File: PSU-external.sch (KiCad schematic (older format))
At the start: 32 parts

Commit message: Added component numbers.
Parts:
- gave numbers to parts that had none: 32
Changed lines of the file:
@@
 $EndDescr
 $Comp
-L CP1 C?
+L CP1 C24
 U 1 1 53688F81
 P 7200 4300
-F 0 "C?" H 7250 4400 50  0000 L CNN
+F 0 "C24" H 7250 4400 50  0000 L CNN
 F 1 "5600u" H 7250 4200 50  0000 L CNN
 F 2 "" H 7200 4300 60  0000 C CNN
@@
 $EndComp
 $Comp
-L C C?
+L C C27
 U 1 1 53688F85
 P 7550 4300
-F 0 "C?" H 7550 4400 40  0000 L CNN
+F 0 "C27" H 7550 4400 40  0000 L CNN
 F 1 "100n" H 7556 4215 40  0000 L CNN
 F 2 "~" H 7588 4150 30  0000 C CNN
@@
 -18V_EXT
 $Comp
-L MC7805C U?
+L MC7805C U12
 U 1 1 53688F96
 P 8000 1050
-F 0 "U?" H 7800 1250 40  0000 C CNN
+F 0 "U12" H 7800 1250 40  0000 C CNN
 F 1 "MC7805C" H 8000 1250 40  0000 L CNN
 F 2 "TO-220" H 8000 1150 30  0000 C CIN
@@
 $EndComp
 $Comp
-L CP1 C?
+L CP1 C23
 U 1 1 53688F97
 P 7150 1500
-F 0 "C?" H 7200 1600 50  0000 L CNN
+F 0 "C23" H 7200 1600 50  0000 L CNN
 F 1 "2700u" H 7200 1400 50  0000 L CNN
 F 2 "" H 7150 1500 60  0000 C CNN
@@
 $EndComp
 $Comp
-L C C?
+L C C26
 U 1 1 53688F98
 P 7550 1500
-F 0 "C?" H 7550 1600 40  0000 L CNN
+F 0 "C26" H 7550 1600 40  0000 L CNN
 F 1 "100n" H 7556 1415 40  0000 L CNN
 F 2 "~" H 7588 1350 30  0000 C CNN
@@
 +20.5V min
 $Comp
-L CP1 C?
+L CP1 C25
 U 1 1 53688FA0
 P 7200 5250
-F 0 "C?" H 7250 5350 50  0000 L CNN
+F 0 "C25" H 7250 5350 50  0000 L CNN
 F 1 "5600u" H 7250 5150 50  0000 L CNN
 F 2 "" H 7200 5250 60  0000 C CNN
@@
 $EndComp
 $Comp
-L C C?
+L C C28
 U 1 1 53688FA4
 P 7550 5250
-F 0 "C?" H 7550 5350 40  0000 L CNN
+F 0 "C28" H 7550 5350 40  0000 L CNN
 F 1 "100n" H 7556 5165 40  0000 L CNN
 F 2 "~" H 7588 5100 30  0000 C CNN
@@
 SAF_GND
 $Comp
-L DIODE D?
+L DIODE D9
 U 1 1 5368E09A
 P 6750 1200
-F 0 "D?" H 6750 1300 40  0000 C CNN
+F 0 "D9" H 6750 1300 40  0000 C CNN
 F 1 "1N4001" H 6750 1100 40  0000 C CNN
 F 2 "~" H 6750 1200 60  0000 C CNN
@@
 $EndComp
 $Comp
-L DIODE D?
+L DIODE D5
 U 1 1 5368E121
 P 6400 1200
-F 0 "D?" H 6400 1300 40  0000 C CNN
+F 0 "D5" H 6400 1300 40  0000 C CNN
 F 1 "1N4001" H 6400 1100 40  0000 C CNN
 F 2 "~" H 6400 1200 60  0000 C CNN
@@
 $EndComp
 $Comp
-L DIODE D?
+L DIODE D6
 U 1 1 5368E163
 P 6400 1800
-F 0 "D?" H 6400 1900 40  0000 C CNN
+F 0 "D6" H 6400 1900 40  0000 C CNN
 F 1 "1N4001" H 6400 1700 40  0000 C CNN
 F 2 "~" H 6400 1800 60  0000 C CNN
@@
 $EndComp
 $Comp
-L DIODE D?
+L DIODE D10
 U 1 1 5368E169
 P 6750 1800
-F 0 "D?" H 6750 1900 40  0000 C CNN
+F 0 "D10" H 6750 1900 40  0000 C CNN
 F 1 "1N4001" H 6750 1700 40  0000 C CNN
 F 2 "~" H 6750 1800 60  0000 C CNN
@@
 $EndComp
 $Comp
-L DIODE D?
+L DIODE D7
 U 1 1 5368E721
 P 6450 3950
-F 0 "D?" H 6450 4050 40  0000 C CNN
+F 0 "D7" H 6450 4050 40  0000 C CNN
 F 1 "RL205" H 6450 3850 40  0000 C CNN
 F 2 "~" H 6450 3950 60  0000 C CNN
@@
 $EndComp
 $Comp
-L DIODE D?
+L DIODE D11
 U 1 1 5368E7AB
 P 6800 3950
-F 0 "D?" H 6800 4050 40  0000 C CNN
+F 0 "D11" H 6800 4050 40  0000 C CNN
 F 1 "RL205" H 6800 3850 40  0000 C CNN
 F 2 "~" H 6800 3950 60  0000 C CNN
@@
 $EndComp
 $Comp
-L DIODE D?
+L DIODE D8
 U 1 1 5368E7B1
 P 6450 5650
-F 0 "D?" H 6450 5750 40  0000 C CNN
+F 0 "D8" H 6450 5750 40  0000 C CNN
 F 1 "RL205" H 6450 5550 40  0000 C CNN
 F 2 "~" H 6450 5650 60  0000 C CNN
@@
 $EndComp
 $Comp
-L DIODE D?
+L DIODE D12
 U 1 1 5368E7B7
 P 6800 5650
-F 0 "D?" H 6800 5750 40  0000 C CNN
+F 0 "D12" H 6800 5750 40  0000 C CNN
 F 1 "RL205" H 6800 5550 40  0000 C CNN
 F 2 "~" H 6800 5650 60  0000 C CNN
@@
 $EndComp
 $Comp
-L C C?
+L C C22
 U 1 1 536984D3
 P 6200 4500
-F 0 "C?" H 6200 4600 40  0000 L CNN
+F 0 "C22" H 6200 4600 40  0000 L CNN
 F 1 "C" H 6206 4415 40  0000 L CNN
 F 2 "~" H 6238 4350 30  0000 C CNN
@@
 $EndComp
 $Comp
-L R R?
+L R R22
 U 1 1 536984E2
 P 6200 5100
-F 0 "R?" V 6280 5100 40  0000 C CNN
+F 0 "R22" V 6280 5100 40  0000 C CNN
 F 1 "R" V 6207 5101 40  0000 C CNN
 F 2 "~" V 6130 5100 30  0000 C CNN
@@
 $EndComp
 $Comp
-L C C?
+L C C21
 U 1 1 5369950E
 P 5800 1200
-F 0 "C?" H 5800 1300 40  0000 L CNN
+F 0 "C21" H 5800 1300 40  0000 L CNN
 F 1 "C" H 5806 1115 40  0000 L CNN
 F 2 "~" H 5838 1050 30  0000 C CNN
@@
 $EndComp
 $Comp
-L R R?
+L R R21
 U 1 1 53699514
 P 5800 1750
-F 0 "R?" V 5880 1750 40  0000 C CNN
+F 0 "R21" V 5880 1750 40  0000 C CNN
 F 1 "R" V 5807 1751 40  0000 C CNN
 F 2 "~" V 5730 1750 30  0000 C CNN
@@
 	6400 2000 8850 2000
 $Comp
-L TRIAD-FS48-750-C2 T?
+L TRIAD-FS48-750-C2 T2
 U 1 1 5369B344
 P 4600 4800
-F 0 "T?" H 4600 5300 70  0000 C CNN
+F 0 "T2" H 4600 5300 70  0000 C CNN
 F 1 "TRIAD-FS48-750-C2" H 4600 4300 70  0000 C CNN
 F 2 "" H 4600 4800 60  0000 C CNN
@@
 $EndComp
 $Comp
-L TRIAD-FS16-400-C2 T?
+L TRIAD-FS16-400-C2 T1
 U 1 1 5369B6AF
 P 4600 1500
-F 0 "T?" H 4600 2000 70  0000 C CNN
+F 0 "T1" H 4600 2000 70  0000 C CNN
 F 1 "TRIAD-FS16-400-C2" H 4600 1000 70  0000 C CNN
 F 2 "" H 4600 1500 60  0000 C CNN
@@
 	5000 1400 5000 1600
 $Comp
-L IEC-C13-SOCKET J?
+L IEC-C13-SOCKET J3
 U 1 1 5369A60D
 P 2600 3700
-F 0 "J?" H 2350 3000 60  0000 L CNN
+F 0 "J3" H 2350 3000 60  0000 L CNN
 F 1 "IEC-C13-SOCKET" H 2350 2900 60  0000 L CNN
 F 2 "~" H 2550 4100 60  0000 C CNN
@@
 Connection ~ 3700 4250
 $Comp
-L LM7918CT U?
+L LM7918CT U14
 U 1 1 5369BF38
 P 8000 5800
-F 0 "U?" H 7800 5600 40  0000 C CNN
+F 0 "U14" H 7800 5600 40  0000 C CNN
 F 1 "LM7918CT" H 8000 5600 40  0000 L CNN
 F 2 "TO-220" H 8000 5700 30  0000 C CIN
@@
 $EndComp
 $Comp
-L LM7818CT U?
+L LM7818CT U13
 U 1 1 5369BF47
 P 8000 3800
-F 0 "U?" H 7800 4000 40  0000 C CNN
+F 0 "U13" H 7800 4000 40  0000 C CNN
 F 1 "LM7818CT" H 8000 4000 40  0000 L CNN
 F 2 "TO-220" H 8000 3900 30  0000 C CIN
@@
 $EndComp
 $Comp
-L DIODE D?
+L DIODE D13
 U 1 1 5369C01A
 P 8000 650
-F 0 "D?" H 8000 750 40  0000 C CNN
+F 0 "D13" H 8000 750 40  0000 C CNN
 F 1 "1N4001" H 8000 550 40  0000 C CNN
 F 2 "~" H 8000 650 60  0000 C CNN
@@
 Connection ~ 7450 1000
 $Comp
-L DIODE D?
+L DIODE D14
 U 1 1 5369C0E9
 P 8000 3400
-F 0 "D?" H 8000 3500 40  0000 C CNN
+F 0 "D14" H 8000 3500 40  0000 C CNN
 F 1 "1N4001" H 8000 3300 40  0000 C CNN
 F 2 "~" H 8000 3400 60  0000 C CNN
@@
 Connection ~ 8500 3750
 $Comp
-L DIODE D?
+L DIODE D15
 U 1 1 5369C1C4
 P 8000 6200
-F 0 "D?" H 8000 6300 40  0000 C CNN
+F 0 "D15" H 8000 6300 40  0000 C CNN
 F 1 "1N4001" H 8000 6100 40  0000 C CNN
 F 2 "~" H 8000 6200 60  0000 C CNN
@@
 Connection ~ 8500 5850
 $Comp
-L CP1 C?
+L CP1 C30
 U 1 1 5369C418
 P 8450 4300
-F 0 "C?" H 8500 4400 50  0000 L CNN
+F 0 "C30" H 8500 4400 50  0000 L CNN
 F 1 "1u" H 8500 4200 50  0000 L CNN
 F 2 "" H 8450 4300 60  0000 C CNN
@@
 Connection ~ 8450 4800
 $Comp
-L CP1 C?
+L CP1 C31
 U 1 1 5369C517
 P 8450 5250
-F 0 "C?" H 8500 5350 50  0000 L CNN
+F 0 "C31" H 8500 5350 50  0000 L CNN
 F 1 "1u" H 8500 5150 50  0000 L CNN
 F 2 "" H 8450 5250 60  0000 C CNN
@@
 Connection ~ 8450 5850
 $Comp
-L CP1 C?
+L CP1 C29
 U 1 1 5369C772
 P 8450 1500
-F 0 "C?" H 8500 1600 50  0000 L CNN
+F 0 "C29" H 8500 1600 50  0000 L CNN
 F 1 "1u" H 8500 1400 50  0000 L CNN
 F 2 "" H 8450 1500 60  0000 C CNN
@@
 	5000 5200 5000 5350
 $Comp
-L SMP50 U?
+L SMP50 U10
 U 1 1 536F40A7
 P 5350 2450
-F 0 "U?" H 5500 2350 60  0000 L CNN
+F 0 "U10" H 5500 2350 60  0000 L CNN
 F 1 "SMP50" H 5500 2250 60  0000 L CNN
 F 2 "" H 5350 2500 60  0000 C CNN
@@
 $EndComp
 $Comp
-L SMP50 U?
+L SMP50 U11
 U 1 1 536F40F8
 P 5400 3650
-F 0 "U?" H 5550 3550 60  0000 L CNN
+F 0 "U11" H 5550 3550 60  0000 L CNN
 F 1 "SMP50" H 5550 3450 60  0000 L CNN
 F 2 "" H 5400 3700 60  0000 C CNN

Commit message: More packages specified; changed the external PSU overvoltage protection devices.
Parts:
- removed U10, U11: SMP50, symbol SMP50
- added U? (x2): P0720ECL, ~, symbol P0720ECL
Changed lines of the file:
@@
 Wire Wire Line
 	5000 5200 5000 5350
-$Comp
-L SMP50 U10
-U 1 1 536F40A7
-P 5350 2450
-F 0 "U10" H 5500 2350 60  0000 L CNN
-F 1 "SMP50" H 5500 2250 60  0000 L CNN
-F 2 "" H 5350 2500 60  0000 C CNN
-F 3 "" H 5350 2500 60  0000 C CNN
-F 4 "497-6526-1-ND" H 5350 2450 60  0001 C CNN "DigiKey"
-	1    5350 2450
-	1    0    0    -1
-$EndComp
-$Comp
-L SMP50 U11
-U 1 1 536F40F8
-P 5400 3650
-F 0 "U11" H 5550 3550 60  0000 L CNN
-F 1 "SMP50" H 5550 3450 60  0000 L CNN
-F 2 "" H 5400 3700 60  0000 C CNN
-F 3 "" H 5400 3700 60  0000 C CNN
-F 4 "497-6526-1-ND" H 5400 3650 60  0001 C CNN "DigiKey"
-	1    5400 3650
-	1    0    0    -1
-$EndComp
 Wire Wire Line
 	2150 3000 8850 3000
@@
 Wire Wire Line
 	5400 3850 5400 4800
+$Comp
+L P0720ECL U?
+U 1 1 537CB1E3
+P 5350 2450
+F 0 "U?" H 5500 2350 60  0000 L CNN
+F 1 "P0720ECL" H 5500 2250 60  0000 L CNN
+F 2 "~" H 5350 2500 60  0000 C CNN
+F 3 "~" H 5350 2500 60  0000 C CNN
+	1    5350 2450
+	1    0    0    -1
+$EndComp
+$Comp
+L P0720ECL U?
+U 1 1 537CB1F0
+P 5400 3650
+F 0 "U?" H 5550 3550 60  0000 L CNN
+F 1 "P0720ECL" H 5550 3450 60  0000 L CNN
+F 2 "~" H 5400 3700 60  0000 C CNN
+F 3 "~" H 5400 3700 60  0000 C CNN
+	1    5400 3650
+	1    0    0    -1
+$EndComp
 $EndSCHEMATC

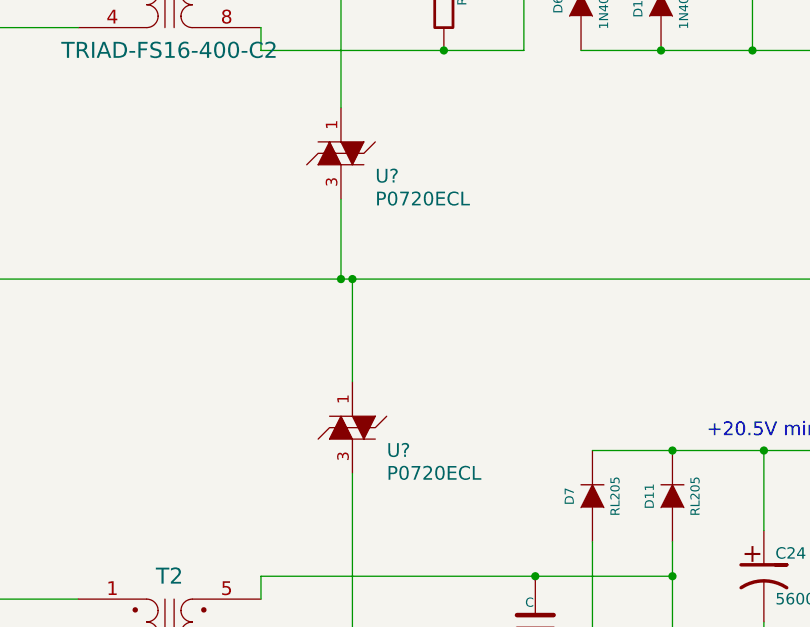
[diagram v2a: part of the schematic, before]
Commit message: More packages specified.
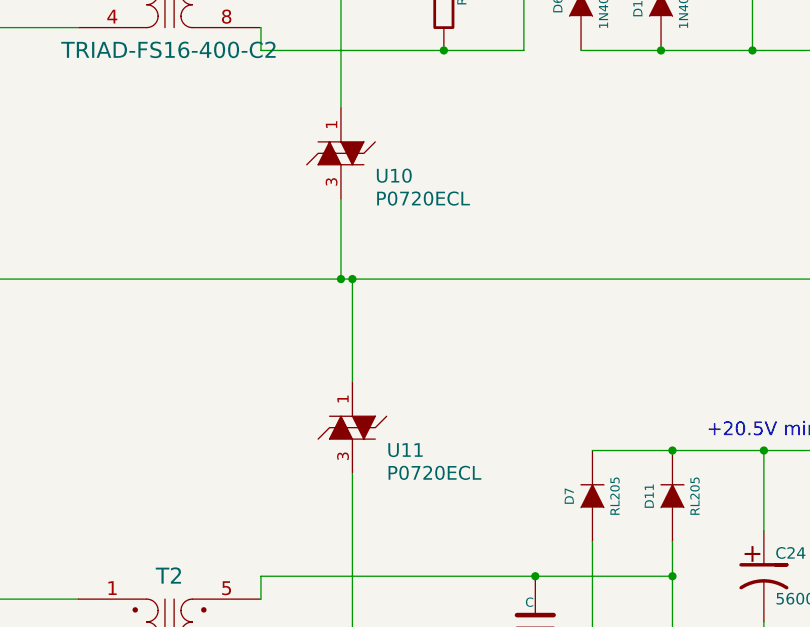
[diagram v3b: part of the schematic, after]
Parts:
- gave numbers to parts that had none: 2
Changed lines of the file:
@@
 	5400 3850 5400 4800
 $Comp
-L P0720ECL U?
+L P0720ECL U10
 U 1 1 537CB1E3
 P 5350 2450
-F 0 "U?" H 5500 2350 60  0000 L CNN
+F 0 "U10" H 5500 2350 60  0000 L CNN
 F 1 "P0720ECL" H 5500 2250 60  0000 L CNN
 F 2 "~" H 5350 2500 60  0000 C CNN
@@
 $EndComp
 $Comp
-L P0720ECL U?
+L P0720ECL U11
 U 1 1 537CB1F0
 P 5400 3650
-F 0 "U?" H 5550 3550 60  0000 L CNN
+F 0 "U11" H 5550 3550 60  0000 L CNN
 F 1 "P0720ECL" H 5550 3450 60  0000 L CNN
 F 2 "~" H 5400 3700 60  0000 C CNN

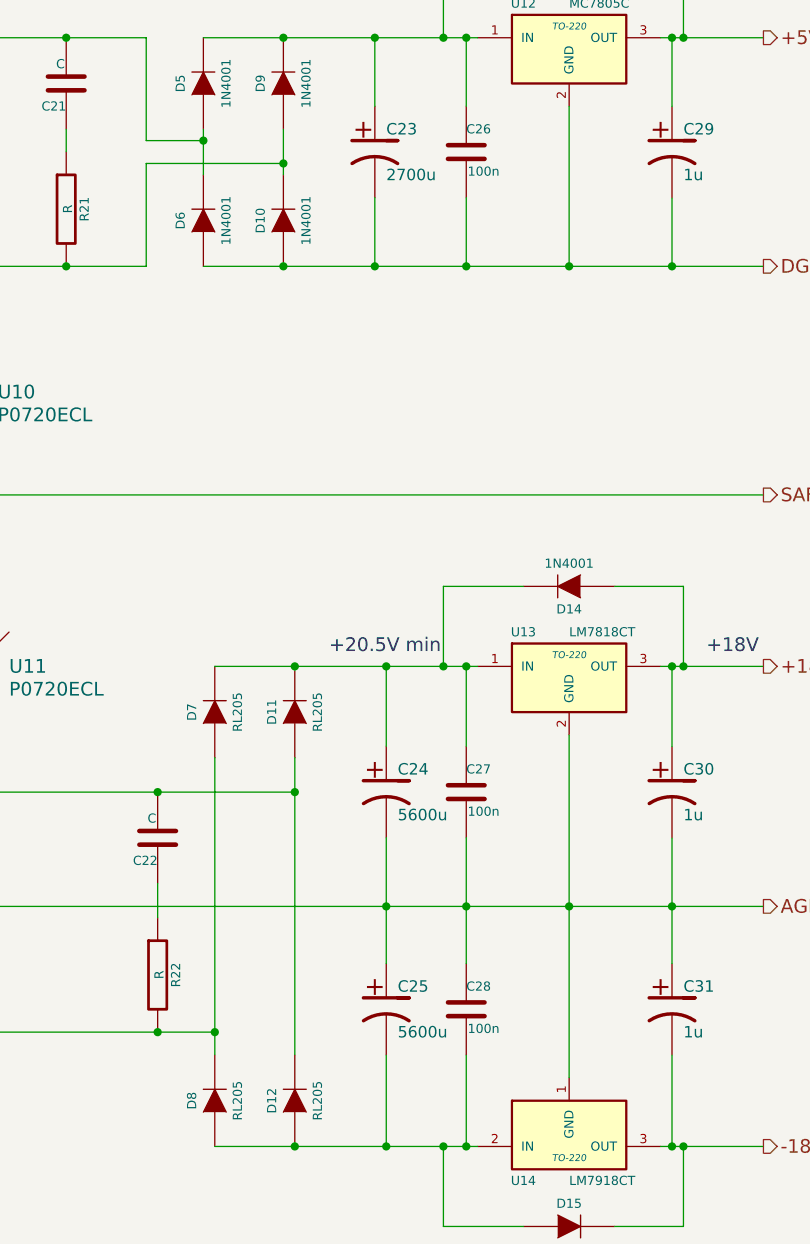
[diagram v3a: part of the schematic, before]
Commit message: Minor schematic mods, started assigning DigiKey part numbers to components.
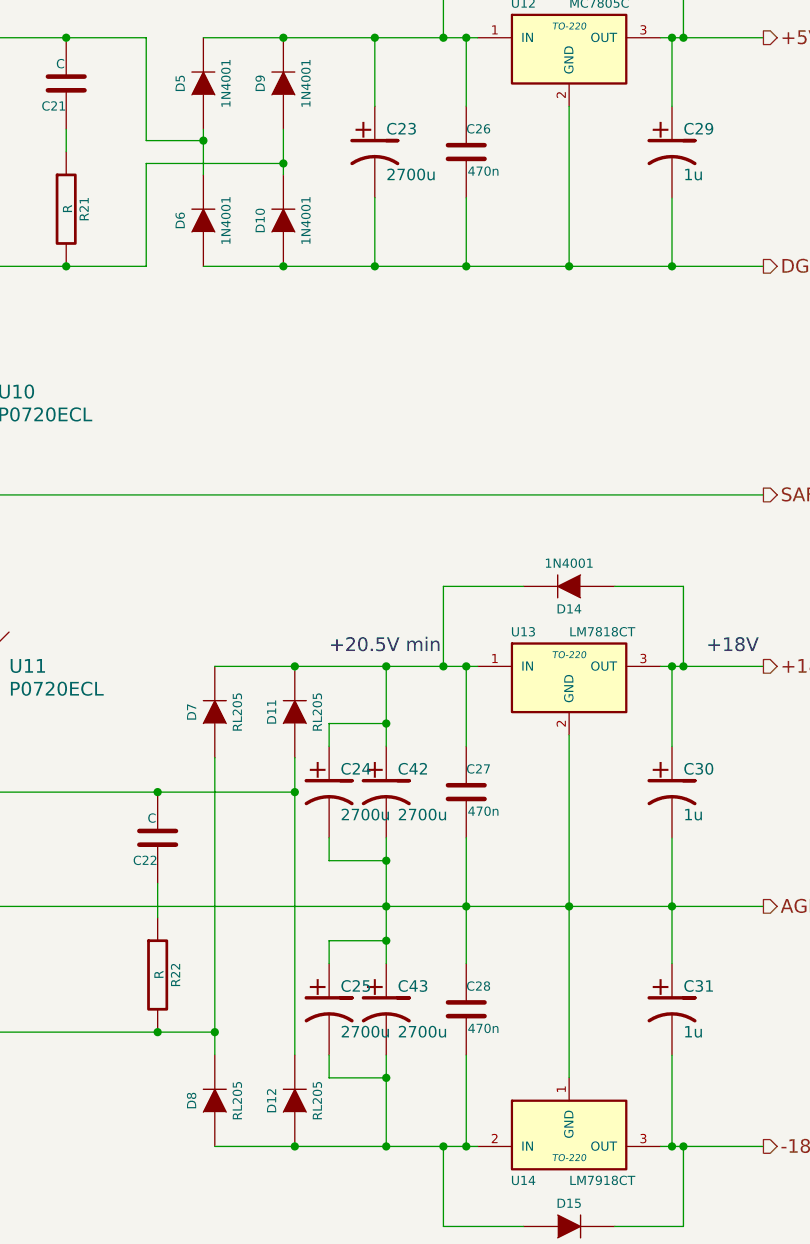
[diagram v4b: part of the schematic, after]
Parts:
- added C42, C43: 2700u, symbol CP1
- C23: DigiKey (none) -> 565-1830-ND
- C24, C25: value 5600u -> 2700u; DigiKey (none) -> 565-1830-ND
- C26, C27, C28: value 100n -> 470n; DigiKey (none) -> 445-8425-ND
- C29, C30, C31: DigiKey (none) -> 478-5812-ND
- D10, D13, D14, D15, D5, D6, D9: DigiKey (none) -> 1N4001-TPMSCT-ND
- D11, D12, D7, D8: DigiKey (none) -> RL205-TPCT-ND
- J3: DigiKey (none) -> CCM1724-ND
- T1: DigiKey (none) -> 237-1504-ND
- U10, U11: DigiKey (none) -> F5278-ND
- U12: DigiKey (none) -> NCP7805TGOS-ND
- U13: DigiKey (none) -> MC7818CTGOS-ND
- U14: DigiKey (none) -> MC7918CTGOS-ND
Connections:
- net AGND_EXT: now also C42.2, C43.1
- net at C24.1, C27.1, D11.2 (K)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: now also C42.1
- net at C25.2, C28.2, D12.1 (A)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: now also C43.2

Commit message: More components specified
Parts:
- added F?: FUSE, ~, symbol FUSE
- renumbered C24 to C23, C25 to C24, C23 to C25, C42 to C26, C43 to C27, C26 to C28, C27 to C29, C28 to C30, C29 to C31, C30 to C32, C31 to C33
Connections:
- no-connect marks 0 -> 2
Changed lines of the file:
@@
 Sheet 3 6
 Title ""
-Date "23 may 2014"
+Date "25 may 2014"
 Rev ""
 Comp ""
@@
 $EndComp
 $Comp
-L CP1 C23
+L CP1 C25
 U 1 1 53688F97
 P 7150 1500
-F 0 "C23" H 7200 1600 50  0000 L CNN
+F 0 "C25" H 7200 1600 50  0000 L CNN
 F 1 "2700u" H 7200 1400 50  0000 L CNN
 F 2 "" H 7150 1500 60  0000 C CNN
@@
 $EndComp
 $Comp
-L C C26
+L C C28
 U 1 1 53688F98
 P 7550 1500
-F 0 "C26" H 7550 1600 40  0000 L CNN
+F 0 "C28" H 7550 1600 40  0000 L CNN
 F 1 "470n" H 7556 1415 40  0000 L CNN
 F 2 "~" H 7588 1350 30  0000 C CNN
@@
 Connection ~ 8450 5850
 $Comp
-L CP1 C29
+L CP1 C31
 U 1 1 5369C772
 P 8450 1500
-F 0 "C29" H 8500 1600 50  0000 L CNN
+F 0 "C31" H 8500 1600 50  0000 L CNN
 F 1 "1u" H 8500 1400 50  0000 L CNN
 F 2 "" H 8450 1500 60  0000 C CNN
@@
 Connection ~ 7200 4600
 $Comp
-L CP1 C24
+L CP1 C23
 U 1 1 537D7104
 P 6950 4300
-F 0 "C24" H 7000 4400 50  0000 L CNN
+F 0 "C23" H 7000 4400 50  0000 L CNN
 F 1 "2700u" H 7000 4200 50  0000 L CNN
 F 2 "" H 6950 4300 60  0000 C CNN
@@
 $EndComp
 $Comp
-L CP1 C42
+L CP1 C26
 U 1 1 537D7111
 P 7200 4300
-F 0 "C42" H 7250 4400 50  0000 L CNN
+F 0 "C26" H 7250 4400 50  0000 L CNN
 F 1 "2700u" H 7250 4200 50  0000 L CNN
 F 2 "" H 7200 4300 60  0000 C CNN
@@
 $EndComp
 $Comp
-L CP1 C25
+L CP1 C24
 U 1 1 537D711E
 P 6950 5250
-F 0 "C25" H 7000 5350 50  0000 L CNN
+F 0 "C24" H 7000 5350 50  0000 L CNN
 F 1 "2700u" H 7000 5150 50  0000 L CNN
 F 2 "" H 6950 5250 60  0000 C CNN
@@
 $EndComp
 $Comp
-L CP1 C43
+L CP1 C27
 U 1 1 537D712B
 P 7200 5250
-F 0 "C43" H 7250 5350 50  0000 L CNN
+F 0 "C27" H 7250 5350 50  0000 L CNN
 F 1 "2700u" H 7250 5150 50  0000 L CNN
 F 2 "" H 7200 5250 60  0000 C CNN
@@
 $EndComp
 $Comp
-L CP1 C30
+L CP1 C32
 U 1 1 537D7387
 P 8450 4300
-F 0 "C30" H 8500 4400 50  0000 L CNN
+F 0 "C32" H 8500 4400 50  0000 L CNN
 F 1 "1u" H 8500 4200 50  0000 L CNN
 F 2 "" H 8450 4300 60  0000 C CNN
@@
 $EndComp
 $Comp
-L CP1 C31
+L CP1 C33
 U 1 1 537D73A0
 P 8450 5250
-F 0 "C31" H 8500 5350 50  0000 L CNN
+F 0 "C33" H 8500 5350 50  0000 L CNN
 F 1 "1u" H 8500 5150 50  0000 L CNN
 F 2 "" H 8450 5250 60  0000 C CNN
@@
 $EndComp
 $Comp
-L C C27
+L C C29
 U 1 1 537D758E
 P 7550 4300
-F 0 "C27" H 7550 4400 40  0000 L CNN
+F 0 "C29" H 7550 4400 40  0000 L CNN
 F 1 "470n" H 7556 4215 40  0000 L CNN
 F 2 "~" H 7588 4150 30  0000 C CNN
@@
 $EndComp
 $Comp
-L C C28
+L C C30
 U 1 1 537D75A7
 P 7550 5250
-F 0 "C28" H 7550 5350 40  0000 L CNN
+F 0 "C30" H 7550 5350 40  0000 L CNN
 F 1 "470n" H 7556 5165 40  0000 L CNN
 F 2 "~" H 7588 5100 30  0000 C CNN
@@
 	1    0    0    -1
 $EndComp
+$Comp
+L FUSE F?
+U 1 1 53819FC7
+P 2550 5000
+F 0 "F?" H 2650 5050 40  0000 C CNN
+F 1 "FUSE" H 2450 4950 40  0000 C CNN
+F 2 "~" H 2550 5000 60  0000 C CNN
+F 3 "~" H 2550 5000 60  0000 C CNN
+F 4 "F1764-ND" H 2550 5000 60  0001 C CNN "DigiKey"
+	1    2550 5000
+	1    0    0    -1
+$EndComp
+NoConn ~ 2300 5000
+NoConn ~ 2800 5000
 $EndSCHEMATC

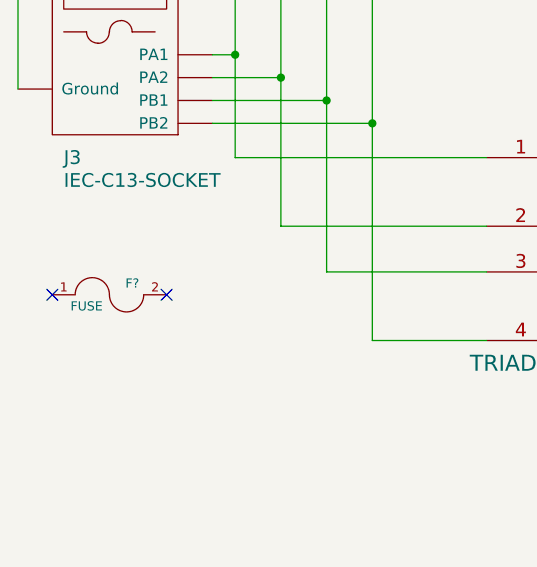
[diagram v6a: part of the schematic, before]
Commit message: Completed component product code specification; started on footprints.
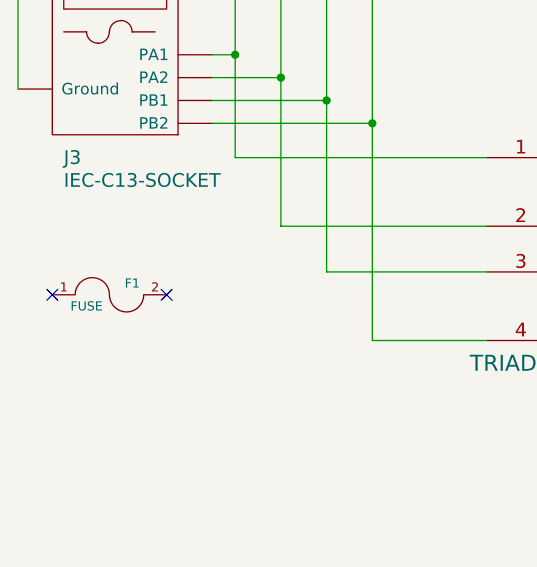
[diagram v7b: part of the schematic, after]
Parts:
- gave numbers to parts that had none: 1
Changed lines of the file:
@@
 LIBS:my-conn
 LIBS:ADC-cache
-EELAYER 27 0
+EELAYER 24 0
 EELAYER END
 $Descr A4 11693 8268
@@
 $EndComp
 $Comp
-L FUSE F?
+L FUSE F1
 U 1 1 53819FC7
 P 2550 5000
-F 0 "F?" H 2650 5050 40  0000 C CNN
+F 0 "F1" H 2650 5050 40  0000 C CNN
 F 1 "FUSE" H 2450 4950 40  0000 C CNN
 F 2 "~" H 2550 5000 60  0000 C CNN

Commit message: More footprint specification and connector additions; almost done.
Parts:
- added P18, P19, P20, P21, P22: CONN_1, symbol CONN_1
- C21, C22, F1, J3, R21, R22, U10, U11: footprint ~ -> (none)
- C23, C24, C25, C26, C27: footprint (none) -> Capacitors_ThroughHole:Capacitor16x25RM7.5
- C28, C29, C30: footprint ~ -> Capacitors_ThroughHole:Capacitor3MMDiscRM2.5
- C31, C32, C33: footprint (none) -> Capacitors_ThroughHole:Capacitor5x6RM2.5
- D10, D13, D14, D15, D5, D6, D9: footprint ~ -> Diodes_ThroughHole:Diode_DO-41_SOD81_Horizontal_RM10
- D11, D12, D7, D8: footprint ~ -> Diodes_ThroughHole:Diode_DO-201AD_Horizontal_RM15
- T1: footprint (none) -> my-trafos:TRIAD_FS16_400_C2
- T2: footprint (none) -> my-trafos:TRIAD_FS48_750_C2
- U12, U13, U14: footprint TO-220 -> Transistors_TO-220:TO-220_Neutral123_Vertical_LargePads
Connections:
- wire segments 88 -> 93
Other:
- moved on the sheet: J3
